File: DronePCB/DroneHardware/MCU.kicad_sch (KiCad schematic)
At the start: 21 parts, among them SW1 SW_SPDT, U1 STM32F401RCT6, Y1 16MHz

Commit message: Aggiornamento Aggiunta della MPU-6050 per test
E' stato fatto uno studio per capire il funzionamento di OMNIBUSF4
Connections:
- net GYRO_INT: now reaches U1.57 (PB5)
- no-connect marks 38 -> 37
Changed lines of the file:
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@@
   (no_connect (at 145.288 104.648))
   (no_connect (at 145.288 107.188))
-  (no_connect (at 145.288 117.348))
   (no_connect (at 145.288 71.628))
   (no_connect (at 112.268 132.588))
@@
       (effects (font (size 1.27 1.27)) (justify left) hide)
     )
+  )
+  (global_label "GYRO_INT" (shape input) (at 145.288 117.348 0) (fields_autoplaced)
+    (effects (font (size 1.27 1.27)) (justify left))
+    (property "Intersheet References" "${INTERSHEET_REFS}" (id 0) (at 156.5306 117.2686 0)
+      (effects (font (size 1.27 1.27)) (justify left) hide)
+    )

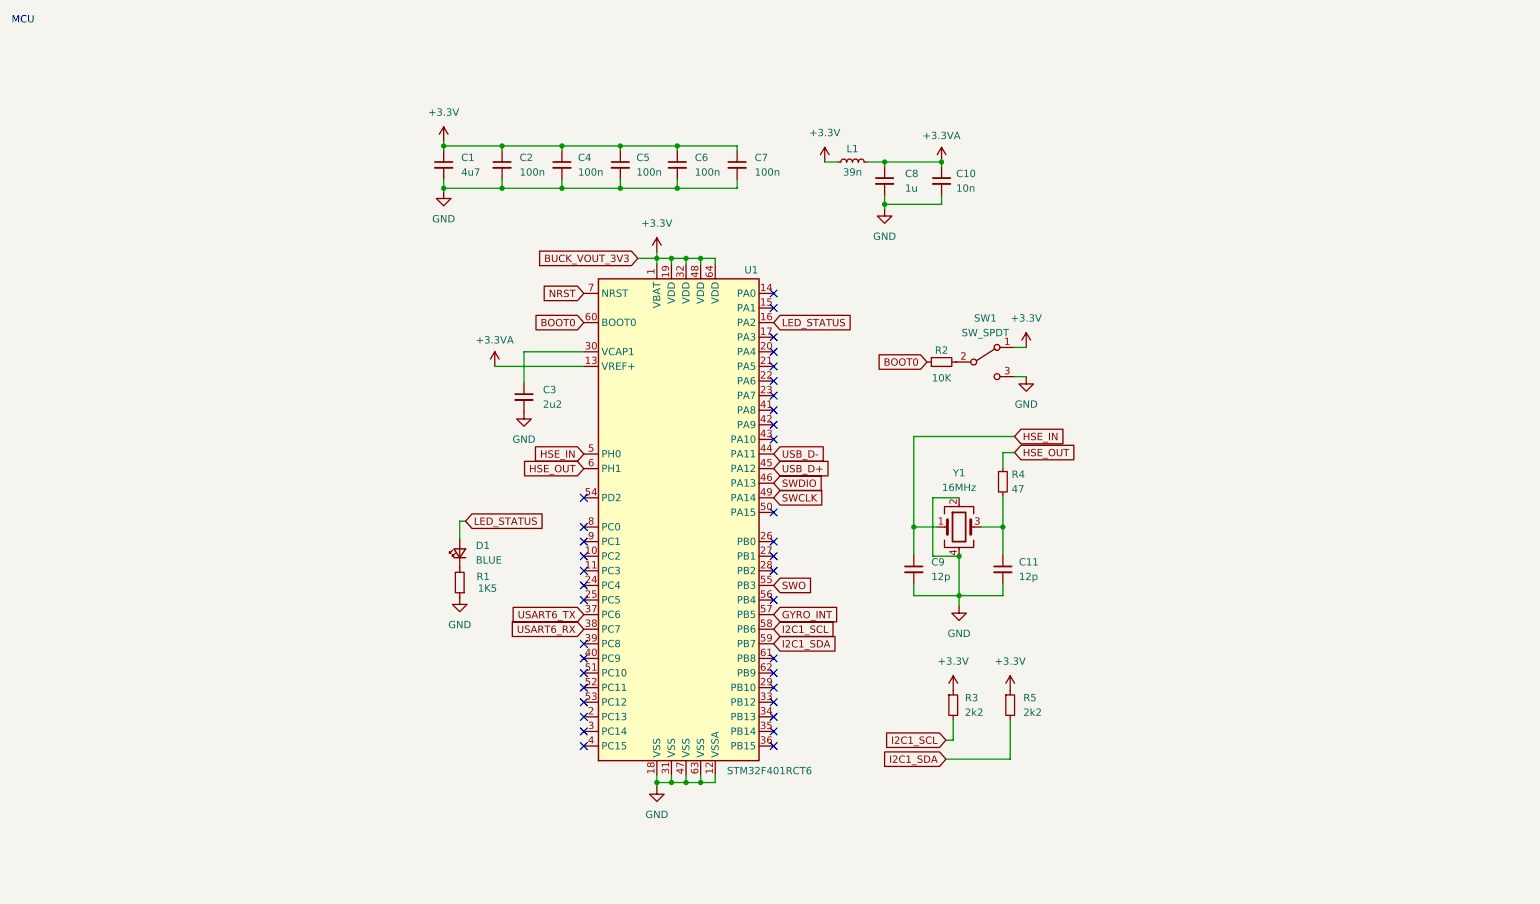
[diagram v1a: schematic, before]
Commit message: Creazione PCB e utilizzo di processore STM32F405
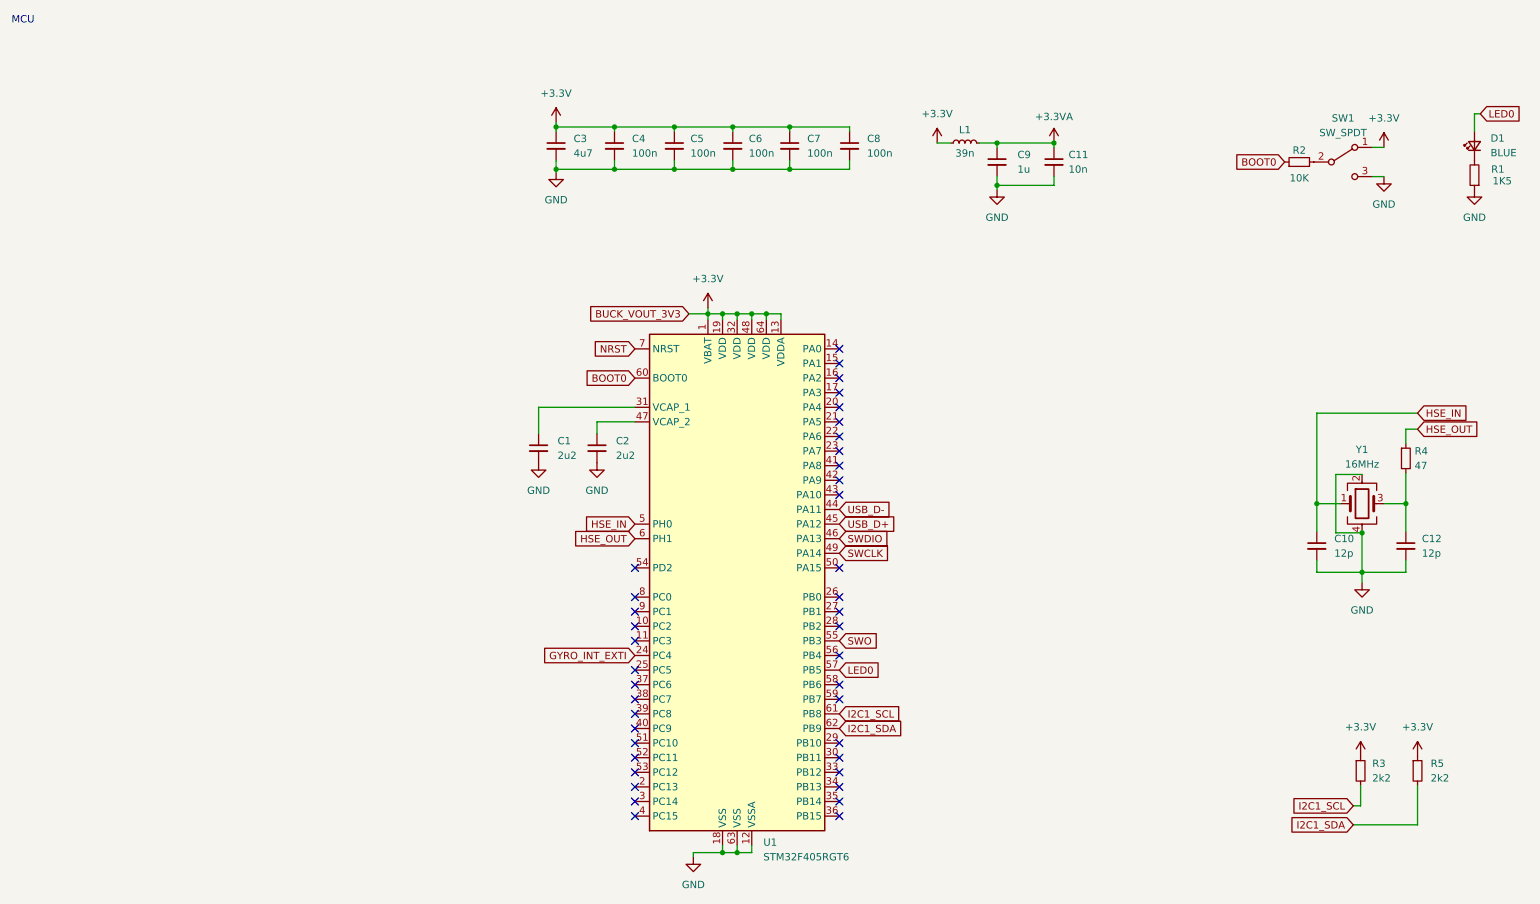
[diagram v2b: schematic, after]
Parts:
- removed C3: 2u2, Capacitor_SMD:C_0603_1608Metric, symbol Device:C_Small
- removed U1: STM32F401RCT6, Package_QFP:LQFP-64_10x10mm_P0.5mm, symbol MCU_ST_STM32F4:STM32F401RCTx
- added C1, C2: 2u2, Capacitor_SMD:C_0603_1608Metric, symbol Device:C_Small
- added U1: STM32F405RGT6, Package_QFP:LQFP-64_10x10mm_P0.5mm, symbol MCU_ST_STM32F4:STM32F405RGTx
- renumbered C9 to C10, C10 to C11, C11 to C12, C1 to C3, C2 to C4, C4 to C5, C5 to C6, C6 to C7, C7 to C8, C8 to C9
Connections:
- net +3V3: now also U1.1 (VBAT), U1.13 (VDDA), U1.19 (VDD), U1.32 (VDD), U1.48 (VDD), U1.64 (VDD)
- net BOOT0: now also U1.60 (BOOT0)
- net GND: now also C1.2, C2.2, U1.12 (VSSA), U1.18 (VSS), U1.63 (VSS)
- net HSE_IN: now also U1.5 (PH0)
- net HSE_OUT: now also U1.6 (PH1)
- net I2C1_SCL: now also U1.61 (PB8)
- net I2C1_SDA: now also U1.62 (PB9)
- net NRST: now also U1.7 (NRST)
- net SWCLK: now also U1.49 (PA14)
- net SWDIO: now also U1.46 (PA13)
- net SWO: now also U1.55 (PB3)
- net USB_D+: now also U1.45 (PA12)
- net USB_D-: now also U1.44 (PA11)
- net LED_STATUS renamed LED0
- net LED0: now also U1.57 (PB5)
- new net: C2.1, U1.47 (VCAP_2)
- new net: C1.1, U1.31 (VCAP_1)
- new net GYRO_INT_EXTI: U1.24 (PC4)
- no-connect marks 37 -> 40
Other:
- moved on the sheet: C10, C11, C12, C3, C4, C5, C6, C7, C8, C9, D1, L1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

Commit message: Da eliminare
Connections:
- net MPU6000_CS_PIN: now reaches U1.20 (PA4)
- no-connect marks 40 -> 39
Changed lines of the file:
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@@
   (no_connect (at 156.718 83.82))
   (no_connect (at 156.718 149.86))
-  (no_connect (at 156.718 81.28))
   (no_connect (at 156.718 88.9))
   (no_connect (at 121.158 119.38))
@@
       (effects (font (size 1.27 1.27)) (justify left) hide)
     )
+  )
+  (global_label "MPU6000_CS_PIN" (shape input) (at 156.718 81.28 0) (fields_autoplaced)
+    (effects (font (size 1.27 1.27)) (justify left))
+    (property "Intersheet References" "${INTERSHEET_REFS}" (id 0) (at 175.6411 81.2006 0)
+      (effects (font (size 1.27 1.27)) (justify left) hide)
+    )

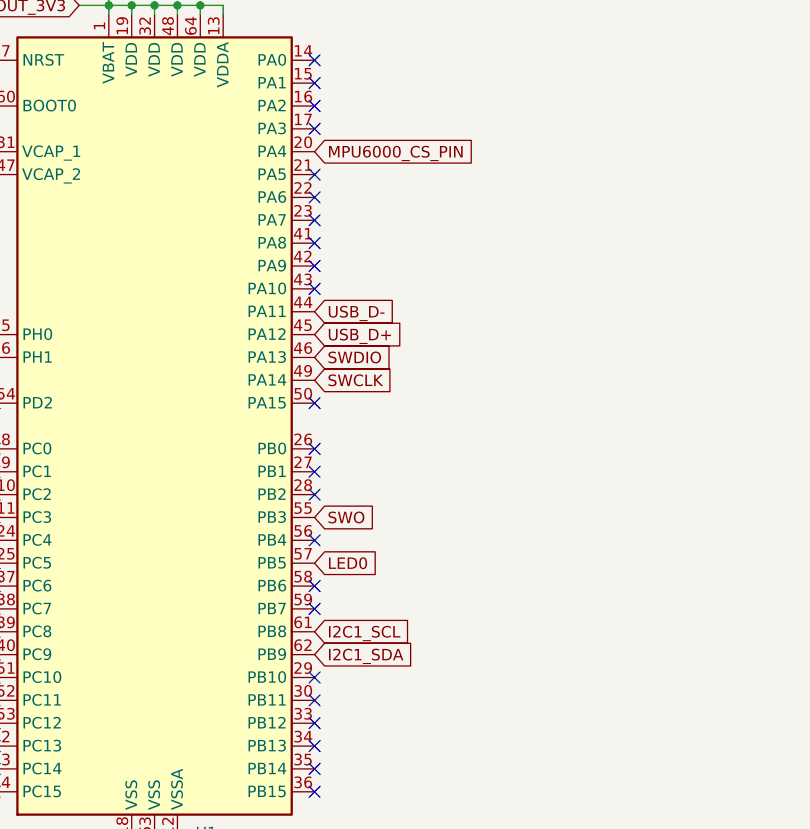
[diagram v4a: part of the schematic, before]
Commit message: Collegamento corretto di mpu-6000
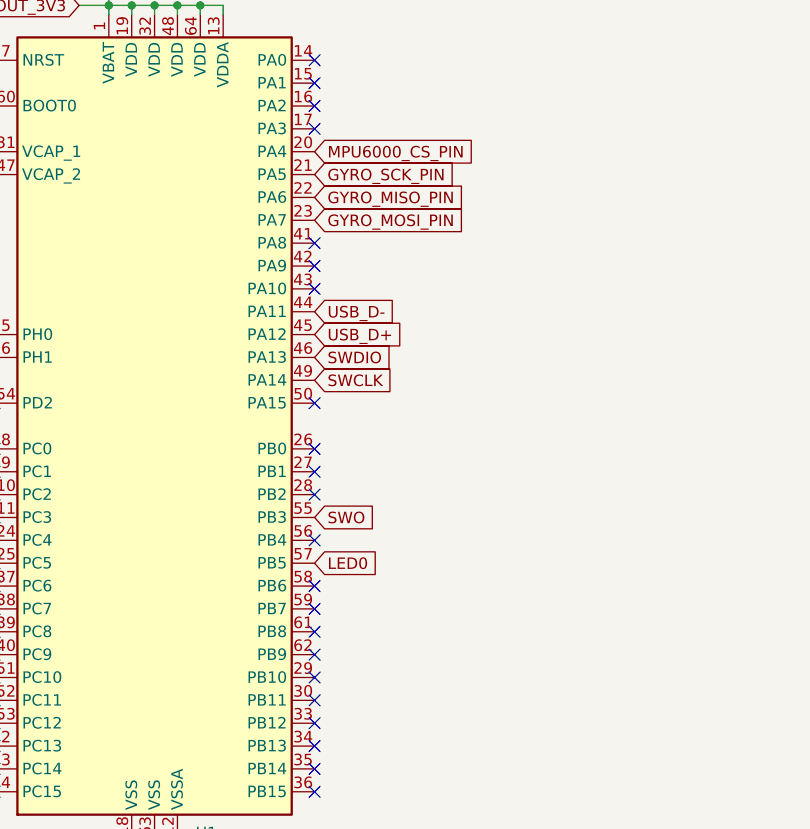
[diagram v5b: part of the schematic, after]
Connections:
- net I2C1_SCL: no longer U1.61 (PB8)
- net I2C1_SDA: no longer U1.62 (PB9)
- net GYRO_SCK_PIN: now reaches U1.21 (PA5)
- net GYRO_MISO_PIN: now reaches U1.22 (PA6)
- net GYRO_MOSI_PIN: now reaches U1.23 (PA7)
- no-connect marks 39 -> 38
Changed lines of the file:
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@@
   (junction (at 144.018 65.024) (diameter 0) (color 0 0 0 0)
   )
-  (no_connect (at 156.718 86.36))
   (no_connect (at 156.718 96.52))
   (no_connect (at 156.718 91.44))
@@
   (no_connect (at 156.718 129.54))
   (no_connect (at 156.718 116.84))
+  (no_connect (at 156.718 134.62))
   (no_connect (at 156.718 73.66))
   (no_connect (at 121.158 144.78))
@@
   (no_connect (at 156.718 152.4))
   (no_connect (at 121.158 142.24))
-  (no_connect (at 156.718 83.82))
   (no_connect (at 156.718 149.86))
-  (no_connect (at 156.718 88.9))
   (no_connect (at 121.158 119.38))
   (no_connect (at 156.718 78.74))
@@
   (no_connect (at 121.158 152.4))
   (no_connect (at 156.718 119.38))
+  (no_connect (at 156.718 137.16))
   (no_connect (at 156.718 144.78))
   (no_connect (at 121.158 129.54))
@@
     )
   )
-  (global_label "I2C1_SDA" (shape input) (at 156.718 137.16 0) (fields_autoplaced)
-    (effects (font (size 1.27 1.27)) (justify left))
-    (property "Intersheet References" "${INTERSHEET_REFS}" (id 0) (at 167.9606 137.0806 0)
+  (global_label "GYRO_MOSI_PIN" (shape input) (at 156.718 88.9 0) (fields_autoplaced)
+    (effects (font (size 1.27 1.27)) (justify left))
+    (property "Intersheet References" "${INTERSHEET_REFS}" (id 0) (at 173.8268 88.8206 0)
       (effects (font (size 1.27 1.27)) (justify left) hide)
     )
@@
     )
   )
+  (global_label "GYRO_MISO_PIN" (shape input) (at 156.718 86.36 0) (fields_autoplaced)
+    (effects (font (size 1.27 1.27)) (justify left))
+    (property "Intersheet References" "${INTERSHEET_REFS}" (id 0) (at 173.8268 86.2806 0)
+      (effects (font (size 1.27 1.27)) (justify left) hide)
+    )
+  )
   (global_label "MPU6000_CS_PIN" (shape input) (at 156.718 81.28 0) (fields_autoplaced)
     (effects (font (size 1.27 1.27)) (justify left))
@@
     )
   )
-  (global_label "I2C1_SCL" (shape input) (at 156.718 134.62 0) (fields_autoplaced)
-    (effects (font (size 1.27 1.27)) (justify left))
-    (property "Intersheet References" "${INTERSHEET_REFS}" (id 0) (at 167.9001 134.5406 0)
-      (effects (font (size 1.27 1.27)) (justify left) hide)
-    )
+  (global_label "GYRO_SCK_PIN" (shape input) (at 156.718 83.82 0) (fields_autoplaced)
+    (effects (font (size 1.27 1.27)) (justify left))
+    (property "Intersheet References" "${INTERSHEET_REFS}" (id 0) (at 172.9801 83.7406 0)
+      (effects (font (size 1.27 1.27)) (justify left) hide)
+    )

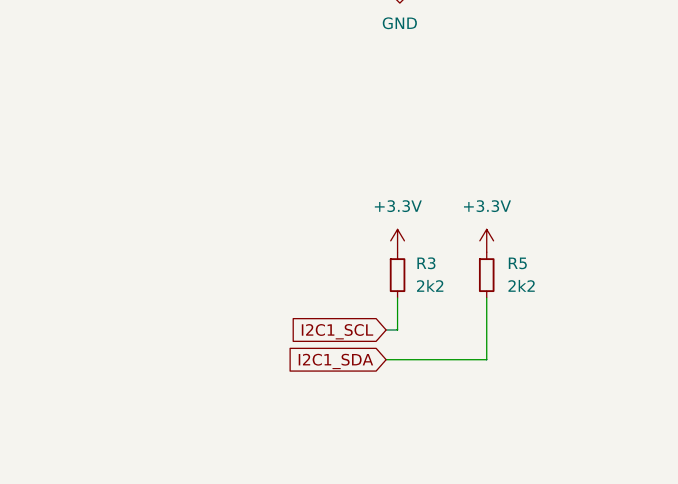
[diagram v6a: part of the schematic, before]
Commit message: Posizionamento di tutte le componenti
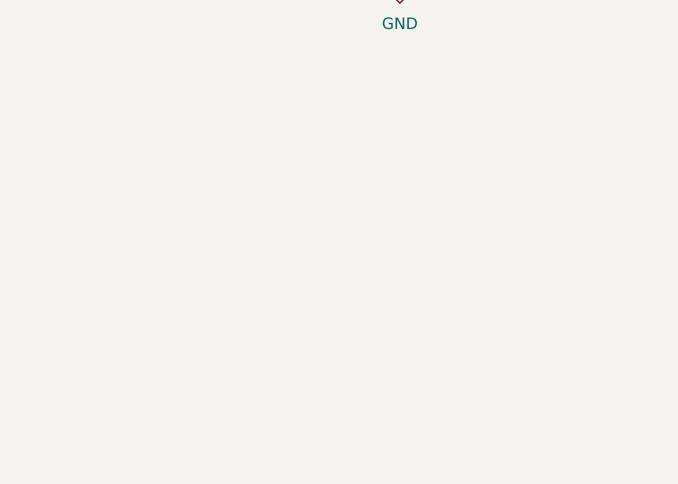
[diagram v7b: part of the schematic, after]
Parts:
- removed R3, R5: 2k2, Resistor_SMD:R_0603_1608Metric, symbol Device:R_Small
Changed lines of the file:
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@@
-    (stroke (width 0) (type default) (color 0 0 0 0))
-  )
-  (wire (pts (xy 247.396 147.066) (xy 247.396 150.622))
     (stroke (width 0) (type default) (color 0 0 0 0))
   )
@@
     (stroke (width 0) (type default) (color 0 0 0 0))
   )
-  (wire (pts (xy 246.126 153.924) (xy 257.302 153.924))
-    (stroke (width 0) (type default) (color 0 0 0 0))
-  )
   (wire (pts (xy 184.15 42.672) (xy 194.056 42.672))
     (stroke (width 0) (type default) (color 0 0 0 0))
@@
     (stroke (width 0) (type default) (color 0 0 0 0))
   )
-  (wire (pts (xy 257.302 153.924) (xy 257.302 147.066))
-    (stroke (width 0) (type default) (color 0 0 0 0))
-  )
   (wire (pts (xy 255.27 85.09) (xy 255.27 87.63))
     (stroke (width 0) (type default) (color 0 0 0 0))
@@
   )
   (wire (pts (xy 247.65 111.76) (xy 247.65 109.982))
-    (stroke (width 0) (type default) (color 0 0 0 0))
-  )
-  (wire (pts (xy 247.396 150.622) (xy 246.126 150.622))
     (stroke (width 0) (type default) (color 0 0 0 0))
   )
@@
   (text "MCU\n" (at 12.7 14.732 0)
     (effects (font (size 1.27 1.27)) (justify left bottom))
-  )
-  (global_label "I2C1_SDA" (shape input) (at 246.126 153.924 180) (fields_autoplaced)
-    (effects (font (size 1.27 1.27)) (justify right))
-    (property "Intersheet References" "${INTERSHEET_REFS}" (id 0) (at 234.8834 154.0034 0)
-      (effects (font (size 1.27 1.27)) (justify right) hide)
-    )
   )
   (global_label "NRST" (shape input) (at 121.158 71.12 180) (fields_autoplaced)
@@
     (property "Intersheet References" "${INTERSHEET_REFS}" (id 0) (at 275.2938 30.1466 0)
       (effects (font (size 1.27 1.27)) (justify left) hide)
-    )
-  )
-  (global_label "I2C1_SCL" (shape input) (at 246.126 150.622 180) (fields_autoplaced)
-    (effects (font (size 1.27 1.27)) (justify right))
-    (property "Intersheet References" "${INTERSHEET_REFS}" (id 0) (at 234.9439 150.7014 0)
-      (effects (font (size 1.27 1.27)) (justify right) hide)
     )
   )
@@
     (pin "1")
   )
-  (symbol (lib_id "Device:R_Small") (at 247.396 144.526 0) (unit 1)
-    (in_bom yes) (on_board yes) (fields_autoplaced)
-    (property "Reference" "R3" (id 0) (at 249.428 143.2559 0)
-      (effects (font (size 1.27 1.27)) (justify left))
-    )
-    (property "Value" "2k2" (id 1) (at 249.428 145.7959 0)
-      (effects (font (size 1.27 1.27)) (justify left))
-    )
-    (property "Footprint" "Resistor_SMD:R_0603_1608Metric" (id 2) (at 247.396 144.526 0)
-      (effects (font (size 1.27 1.27)) hide)
-    )
-    (property "Datasheet" "~" (id 3) (at 247.396 144.526 0)
-      (effects (font (size 1.27 1.27)) hide)
-    )
-    (property "LCSC Part #" "C4190" (id 4) (at 247.396 144.526 0)
-      (effects (font (size 1.27 1.27)) hide)
-    )
-    (pin "1")
-    (pin "2")
-  )
   (symbol (lib_id "power:GND") (at 114.554 90.932 0) (unit 1)
     (in_bom yes) (on_board yes) (fields_autoplaced)
@@
     (pin "1")
     (pin "2")
-  )
-  (symbol (lib_id "power:+3.3V") (at 257.302 141.986 0) (unit 1)
-    (in_bom yes) (on_board yes) (fields_autoplaced)
-    (property "Reference" "#PWR013" (id 0) (at 257.302 145.796 0)
-      (effects (font (size 1.27 1.27)) hide)
-    )
-    (property "Value" "+3.3V" (id 1) (at 257.302 136.906 0))
-    (property "Footprint" "" (id 2) (at 257.302 141.986 0)
-      (effects (font (size 1.27 1.27)) hide)
-    )
-    (property "Datasheet" "" (id 3) (at 257.302 141.986 0)
-      (effects (font (size 1.27 1.27)) hide)
-    )
-    (pin "1")
   )
   (symbol (lib_id "power:+3.3V") (at 251.46 36.068 0) (unit 1)
@@
     (pin "2")
   )
-  (symbol (lib_id "power:+3.3V") (at 247.396 141.986 0) (unit 1)
-    (in_bom yes) (on_board yes) (fields_autoplaced)
-    (property "Reference" "#PWR011" (id 0) (at 247.396 145.796 0)
-      (effects (font (size 1.27 1.27)) hide)
-    )
-    (property "Value" "+3.3V" (id 1) (at 247.396 136.906 0))
-    (property "Footprint" "" (id 2) (at 247.396 141.986 0)
-      (effects (font (size 1.27 1.27)) hide)
-    )
-    (property "Datasheet" "" (id 3) (at 247.396 141.986 0)
-      (effects (font (size 1.27 1.27)) hide)
-    )
-    (pin "1")
-  )
   (symbol (lib_id "Device:C_Small") (at 184.15 38.608 0) (unit 1)
     (in_bom yes) (on_board yes) (fields_autoplaced)
@@
       (effects (font (size 1.27 1.27)) hide)
     )
-    (pin "1")
-    (pin "2")
-  )
-  (symbol (lib_id "Device:R_Small") (at 257.302 144.526 0) (unit 1)
-    (in_bom yes) (on_board yes) (fields_autoplaced)
-    (property "Reference" "R5" (id 0) (at 259.588 143.2559 0)
-      (effects (font (size 1.27 1.27)) (justify left))
-    )
-    (property "Value" "2k2" (id 1) (at 259.588 145.7959 0)
-      (effects (font (size 1.27 1.27)) (justify left))
-    )
-    (property "Footprint" "Resistor_SMD:R_0603_1608Metric" (id 2) (at 257.302 144.526 0)
-      (effects (font (size 1.27 1.27)) hide)
-    )
-    (property "Datasheet" "~" (id 3) (at 257.302 144.526 0)
-      (effects (font (size 1.27 1.27)) hide)
-    )
-    (property "LCSC Part #" "C4190" (id 4) (at 257.302 144.526 0)
-      (effects (font (size 1.27 1.27)) hide)
-    )
